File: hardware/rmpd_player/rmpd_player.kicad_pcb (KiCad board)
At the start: 2 copper layers, 59 parts, among them J1 POWER, J2 PROG, J3 LINE_OUT_INT, J4 LINE_OUT, J5 MICRO_SD, Q1 BC848, Q2 BC848, Q3 BC858, Q4 BC858, U1 DS3231M, U2 VS1011E, U3 LM1117-3.3, U4 ESP32-WROOM, Y1 12.288MHz

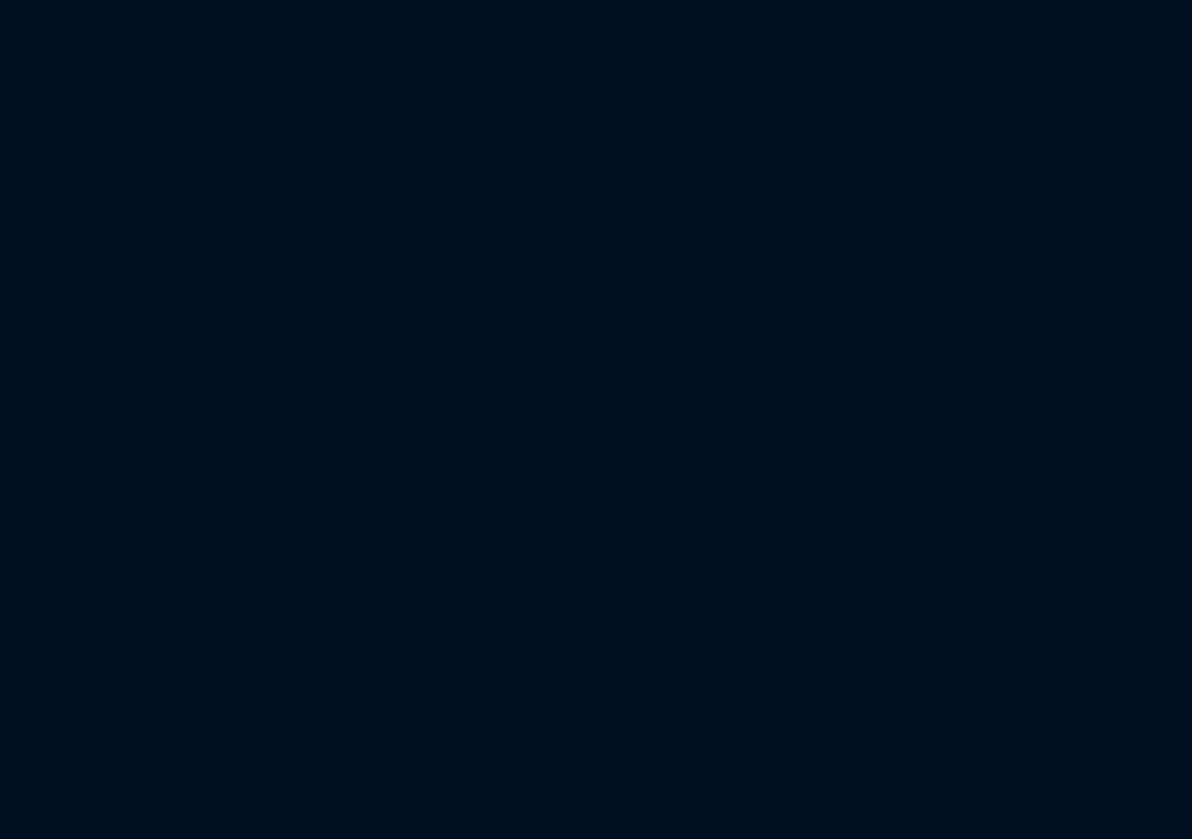
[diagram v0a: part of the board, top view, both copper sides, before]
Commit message: schematic op amp buffer; bom list
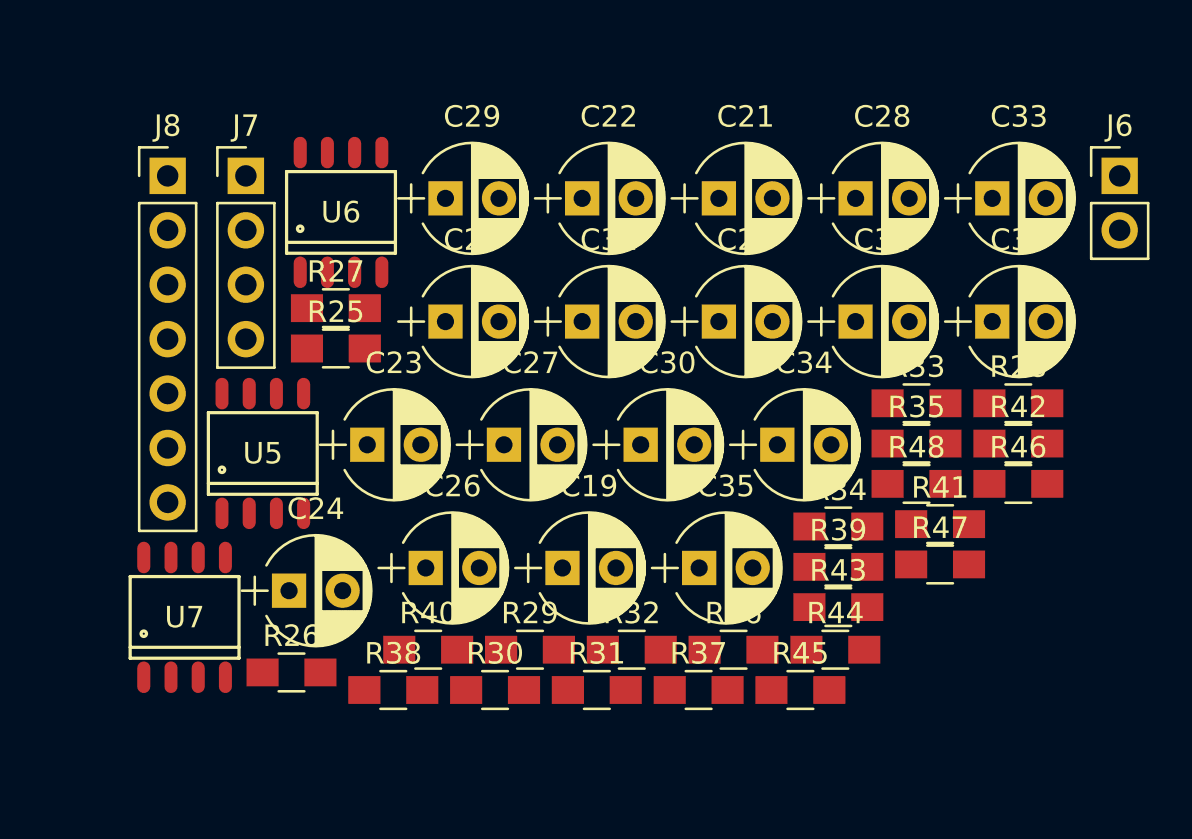
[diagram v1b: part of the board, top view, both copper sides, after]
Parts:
- added C19: 10.0, Capacitors_THT:CP_Radial_D5.0mm_P2.50mm, F.Cu at (195.5, 108.4)
- added C20: 10.0, Capacitors_THT:CP_Radial_D5.0mm_P2.50mm, F.Cu at (190.1, 96.9)
- added C21: 10.0, Capacitors_THT:CP_Radial_D5.0mm_P2.50mm, F.Cu at (202.8, 91.1)
- added C22: 10.0, Capacitors_THT:CP_Radial_D5.0mm_P2.50mm, F.Cu at (196.4, 91.1)
- added C23: 10.0, Capacitors_THT:CP_Radial_D5.0mm_P2.50mm, F.Cu at (186.4, 102.6)
- added C24: 10.0, Capacitors_THT:CP_Radial_D5.0mm_P2.50mm, F.Cu at (182.8, 109.5)
- added C25: 10.0, Capacitors_THT:CP_Radial_D5.0mm_P2.50mm, F.Cu at (202.8, 96.9)
- added C26: 10.0, Capacitors_THT:CP_Radial_D5.0mm_P2.50mm, F.Cu at (189.1, 108.4)
- added C27: 10.0, Capacitors_THT:CP_Radial_D5.0mm_P2.50mm, F.Cu at (192.8, 102.6)
- added C28: 10.0, Capacitors_THT:CP_Radial_D5.0mm_P2.50mm, F.Cu at (209.2, 91.1)
- added C29: 10.0, Capacitors_THT:CP_Radial_D5.0mm_P2.50mm, F.Cu at (190.1, 91.1)
- added C30: 10.0, Capacitors_THT:CP_Radial_D5.0mm_P2.50mm, F.Cu at (199.2, 102.6)
- added C31: 10.0, Capacitors_THT:CP_Radial_D5.0mm_P2.50mm, F.Cu at (196.4, 96.9)
- added C32: 10.0, Capacitors_THT:CP_Radial_D5.0mm_P2.50mm, F.Cu at (209.2, 96.9)
- added C33: 10.0, Capacitors_THT:CP_Radial_D5.0mm_P2.50mm, F.Cu at (215.6, 91.1)
- added C34: 10.0, Capacitors_THT:CP_Radial_D5.0mm_P2.50mm, F.Cu at (205.5, 102.6)
- added C35: 10.0, Capacitors_THT:CP_Radial_D5.0mm_P2.50mm, F.Cu at (201.9, 108.4)
- added C36: 10.0, Capacitors_THT:CP_Radial_D5.0mm_P2.50mm, F.Cu at (215.6, 96.9)
- added J6: POWER_INT, Pin_Headers:Pin_Header_Straight_1x02_Pitch2.54mm, F.Cu at (221.5, 90.1)
- added J7: LINE_OUT_INT_2, Pin_Headers:Pin_Header_Straight_1x04_Pitch2.54mm, F.Cu at (180.7, 90.1)
- added J8: RESERV, Pin_Headers:Pin_Header_Straight_1x07_Pitch2.54mm, F.Cu at (177.1, 90.1)
- added R25: 4k7, Resistors_SMD:R_0805_HandSoldering, F.Cu at (184.9, 98.1)
- added R26: 4k7, Resistors_SMD:R_0805_HandSoldering, F.Cu at (182.9, 113.3)
- added R27: 4k7, Resistors_SMD:R_0805_HandSoldering, F.Cu at (184.9, 96.3)
- added R28: 4k7, Resistors_SMD:R_0805_HandSoldering, F.Cu at (216.8, 100.7)
- added R29: 4k7, Resistors_SMD:R_0805_HandSoldering, F.Cu at (194.0, 112.2)
- added R30: 4k7, Resistors_SMD:R_0805_HandSoldering, F.Cu at (192.4, 114.1)
- added R31: 4k7, Resistors_SMD:R_0805_HandSoldering, F.Cu at (197.1, 114.1)
- added R32: 4k7, Resistors_SMD:R_0805_HandSoldering, F.Cu at (198.7, 112.2)
- added R33: 4k7, Resistors_SMD:R_0805_HandSoldering, F.Cu at (212.0, 100.7)
- added R34: 4k7, Resistors_SMD:R_0805_HandSoldering, F.Cu at (208.4, 106.5)
- added R35: 4k7, Resistors_SMD:R_0805_HandSoldering, F.Cu at (212.0, 102.6)
- added R36: 4k7, Resistors_SMD:R_0805_HandSoldering, F.Cu at (203.5, 112.2)
- added R37: 10k, Resistors_SMD:R_0805_HandSoldering, F.Cu at (201.9, 114.1)
- added R38: 10k, Resistors_SMD:R_0805_HandSoldering, F.Cu at (187.6, 114.1)
- added R39: 10k, Resistors_SMD:R_0805_HandSoldering, F.Cu at (208.4, 108.3)
- added R40: 10k, Resistors_SMD:R_0805_HandSoldering, F.Cu at (189.2, 112.2)
- added R41: 10k, Resistors_SMD:R_0805_HandSoldering, F.Cu at (213.1, 106.3)
- added R42: 10k, Resistors_SMD:R_0805_HandSoldering, F.Cu at (216.8, 102.6)
- added R43: 100k, Resistors_SMD:R_0805_HandSoldering, F.Cu at (208.4, 110.2)
- added R44: 100k, Resistors_SMD:R_0805_HandSoldering, F.Cu at (208.2, 112.2)
- added R45: 100k, Resistors_SMD:R_0805_HandSoldering, F.Cu at (206.6, 114.1)
- added R46: 100k, Resistors_SMD:R_0805_HandSoldering, F.Cu at (216.8, 104.5)
- added R47: 100k, Resistors_SMD:R_0805_HandSoldering, F.Cu at (213.1, 108.2)
- added R48: 100k, Resistors_SMD:R_0805_HandSoldering, F.Cu at (212.0, 104.5)
- added U5: RC4558, Power_Integrations:SO-8, F.Cu at (181.5, 103.0)
- added U6: RC4558, Power_Integrations:SO-8, F.Cu at (185.2, 91.8)
- added U7: RC4558, Power_Integrations:SO-8, F.Cu at (177.9, 110.7)
- J3: value LINE_OUT_INT -> LINE_OUT_INT_1
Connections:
- net Net-(C12-Pad1) renamed 5V
- C17 pad 2: Net-(C17-Pad2) -> OUT_R
- C18 pad 2: Net-(C18-Pad2) -> OUT_L
- J3 pad 1: Net-(C18-Pad2) -> Net-(C33-Pad2)
- J3 pad 4: Net-(C17-Pad2) -> Net-(C34-Pad2)
- J4 pad 1: Net-(C17-Pad2) -> Net-(C35-Pad2)
- J4 pad 2: Net-(C18-Pad2) -> Net-(C36-Pad2)
- Q1 pad 3: Net-(C17-Pad2) -> OUT_R
- Q2 pad 3: Net-(C18-Pad2) -> OUT_L
- R13 pad 1: Net-(C18-Pad2) -> OUT_L
- R14 pad 1: Net-(C17-Pad2) -> OUT_R
- R23 pad 1: TRANSIENT_MUTE -> Net-(Q4-Pad1)
- R23 pad 2: Net-(Q4-Pad1) -> TRANSIENT_MUTE
- R24 pad 1: TRANSIENT_MUTE -> VDD
- R24 pad 2: VDD -> TRANSIENT_MUTE

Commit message: op amps caps
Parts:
- added C37: 100n, Capacitors_SMD:C_0805_HandSoldering, F.Cu at (182.1, 78.4)
- added C38: 100n, Capacitors_SMD:C_0805_HandSoldering, F.Cu at (182.1, 80.2)
- added C39: 100n, Capacitors_SMD:C_0805_HandSoldering, F.Cu at (186.7, 78.4)
- D1: footprint Diodes_SMD:D_0805 -> Diodes_THT:D_A-405_P7.62mm_Horizontal
- moved D1 12.7 mm to (161.9, 86.2)
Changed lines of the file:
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@@
     (tracks 0)
     (zones 0)
-    (modules 107)
+    (modules 110)
     (nets 89)
   )
@@
     )
   )
-  (module Diodes_SMD:D_0805 (layer F.Cu)
-    (at 157.108001 97.937001)
-    (descr "Diode SMD in 0805 package http://datasheets.avx.com/schottky.pdf")
-    (tags "smd diode")
-    (attr smd)
-    (fp_text reference D1 (at 0 -1.6) (layer F.SilkS)
-      (effects (font (size 1 1) (thickness 0.15)))
-    )
-    (fp_text value 5.1V (at 0 1.7) (layer F.Fab)
-      (effects (font (size 1 1) (thickness 0.15)))
-    )
-    (fp_text user %R (at 0 -1.6) (layer F.Fab)
-      (effects (font (size 1 1) (thickness 0.15)))
-    )
-    (fp_line (start -1.6 -0.8) (end -1.6 0.8) (layer F.SilkS) (width 0.12))
-    (fp_line (start -1.7 0.88) (end -1.7 -0.88) (layer F.CrtYd) (width 0.05))
-    (fp_line (start 1.7 0.88) (end -1.7 0.88) (layer F.CrtYd) (width 0.05))
-    (fp_line (start 1.7 -0.88) (end 1.7 0.88) (layer F.CrtYd) (width 0.05))
-    (fp_line (start -1.7 -0.88) (end 1.7 -0.88) (layer F.CrtYd) (width 0.05))
-    (fp_line (start 0.2 0) (end 0.4 0) (layer F.Fab) (width 0.1))
-    (fp_line (start -0.1 0) (end -0.3 0) (layer F.Fab) (width 0.1))
-    (fp_line (start -0.1 -0.2) (end -0.1 0.2) (layer F.Fab) (width 0.1))
-    (fp_line (start 0.2 0.2) (end 0.2 -0.2) (layer F.Fab) (width 0.1))
-    (fp_line (start -0.1 0) (end 0.2 0.2) (layer F.Fab) (width 0.1))
-    (fp_line (start 0.2 -0.2) (end -0.1 0) (layer F.Fab) (width 0.1))
-    (fp_line (start -1 0.65) (end -1 -0.65) (layer F.Fab) (width 0.1))
-    (fp_line (start 1 0.65) (end -1 0.65) (layer F.Fab) (width 0.1))
-    (fp_line (start 1 -0.65) (end 1 0.65) (layer F.Fab) (width 0.1))
-    (fp_line (start -1 -0.65) (end 1 -0.65) (layer F.Fab) (width 0.1))
-    (fp_line (start -1.6 0.8) (end 1 0.8) (layer F.SilkS) (width 0.12))
-    (fp_line (start -1.6 -0.8) (end 1 -0.8) (layer F.SilkS) (width 0.12))
-    (pad 1 smd rect (at -1.05 0) (size 0.8 0.9) (layers F.Cu F.Paste F.Mask)
-      (net 55 5V))
-    (pad 2 smd rect (at 1.05 0) (size 0.8 0.9) (layers F.Cu F.Paste F.Mask)
-      (net 2 GND))
-    (model ${KISYS3DMOD}/Diodes_SMD.3dshapes/D_0805.wrl
-      (at (xyz 0 0 0))
-      (scale (xyz 1 1 1))
-      (rotate (xyz 0 0 0))
-    )
-  )
   (module Fuse_Holders_and_Fuses:Fuse_SMD1206_HandSoldering (layer F.Cu)
     (at 100.288 130.627001)
@@
       (net 78 "Net-(C35-Pad1)"))
   )
+  (module Capacitors_SMD:C_0805_HandSoldering (layer F.Cu)
+    (at 182.107001 78.380001)
+    (descr "Capacitor SMD 0805, hand soldering")
+    (tags "capacitor 0805")
+    (attr smd)
+    (fp_text reference C37 (at 0 -1.75) (layer F.SilkS)
+      (effects (font (size 1 1) (thickness 0.15)))
+    )
+    (fp_text value 100n (at 0 1.75) (layer F.Fab)
+      (effects (font (size 1 1) (thickness 0.15)))
+    )
+    (fp_line (start 2.25 0.87) (end -2.25 0.87) (layer F.CrtYd) (width 0.05))
+    (fp_line (start 2.25 0.87) (end 2.25 -0.88) (layer F.CrtYd) (width 0.05))
+    (fp_line (start -2.25 -0.88) (end -2.25 0.87) (layer F.CrtYd) (width 0.05))
+    (fp_line (start -2.25 -0.88) (end 2.25 -0.88) (layer F.CrtYd) (width 0.05))
+    (fp_line (start -0.5 0.85) (end 0.5 0.85) (layer F.SilkS) (width 0.12))
+    (fp_line (start 0.5 -0.85) (end -0.5 -0.85) (layer F.SilkS) (width 0.12))
+    (fp_line (start -1 -0.62) (end 1 -0.62) (layer F.Fab) (width 0.1))
+    (fp_line (start 1 -0.62) (end 1 0.62) (layer F.Fab) (width 0.1))
+    (fp_line (start 1 0.62) (end -1 0.62) (layer F.Fab) (width 0.1))
+    (fp_line (start -1 0.62) (end -1 -0.62) (layer F.Fab) (width 0.1))
+    (fp_text user %R (at 0 -1.75) (layer F.Fab)
+      (effects (font (size 1 1) (thickness 0.15)))
+    )
+    (pad 2 smd rect (at 1.25 0) (size 1.5 1.25) (layers F.Cu F.Paste F.Mask)
+      (net 2 GND))
+    (pad 1 smd rect (at -1.25 0) (size 1.5 1.25) (layers F.Cu F.Paste F.Mask)
+      (net 55 5V))
+    (model Capacitors_SMD.3dshapes/C_0805.wrl
+      (at (xyz 0 0 0))
+      (scale (xyz 1 1 1))
+      (rotate (xyz 0 0 0))
+    )
+  )
+  (module Capacitors_SMD:C_0805_HandSoldering (layer F.Cu)
+    (at 182.107001 80.200001)
+    (descr "Capacitor SMD 0805, hand soldering")
+    (tags "capacitor 0805")
+    (attr smd)
+    (fp_text reference C38 (at 0 -1.75) (layer F.SilkS)
+      (effects (font (size 1 1) (thickness 0.15)))
+    )
+    (fp_text value 100n (at 0 1.75) (layer F.Fab)
+      (effects (font (size 1 1) (thickness 0.15)))
+    )
+    (fp_text user %R (at 0 -1.75) (layer F.Fab)
+      (effects (font (size 1 1) (thickness 0.15)))
+    )
+    (fp_line (start -1 0.62) (end -1 -0.62) (layer F.Fab) (width 0.1))
+    (fp_line (start 1 0.62) (end -1 0.62) (layer F.Fab) (width 0.1))
+    (fp_line (start 1 -0.62) (end 1 0.62) (layer F.Fab) (width 0.1))
+    (fp_line (start -1 -0.62) (end 1 -0.62) (layer F.Fab) (width 0.1))
+    (fp_line (start 0.5 -0.85) (end -0.5 -0.85) (layer F.SilkS) (width 0.12))
+    (fp_line (start -0.5 0.85) (end 0.5 0.85) (layer F.SilkS) (width 0.12))
+    (fp_line (start -2.25 -0.88) (end 2.25 -0.88) (layer F.CrtYd) (width 0.05))
+    (fp_line (start -2.25 -0.88) (end -2.25 0.87) (layer F.CrtYd) (width 0.05))
+    (fp_line (start 2.25 0.87) (end 2.25 -0.88) (layer F.CrtYd) (width 0.05))
+    (fp_line (start 2.25 0.87) (end -2.25 0.87) (layer F.CrtYd) (width 0.05))
+    (pad 1 smd rect (at -1.25 0) (size 1.5 1.25) (layers F.Cu F.Paste F.Mask)
+      (net 55 5V))
+    (pad 2 smd rect (at 1.25 0) (size 1.5 1.25) (layers F.Cu F.Paste F.Mask)
+      (net 2 GND))
+    (model Capacitors_SMD.3dshapes/C_0805.wrl
+      (at (xyz 0 0 0))
+      (scale (xyz 1 1 1))
+      (rotate (xyz 0 0 0))
+    )
+  )
+  (module Capacitors_SMD:C_0805_HandSoldering (layer F.Cu)
+    (at 186.657001 78.380001)
+    (descr "Capacitor SMD 0805, hand soldering")
+    (tags "capacitor 0805")
+    (attr smd)
+    (fp_text reference C39 (at 0 -1.75) (layer F.SilkS)
+      (effects (font (size 1 1) (thickness 0.15)))
+    )
+    (fp_text value 100n (at 0 1.75) (layer F.Fab)
+      (effects (font (size 1 1) (thickness 0.15)))
+    )
+    (fp_line (start 2.25 0.87) (end -2.25 0.87) (layer F.CrtYd) (width 0.05))
+    (fp_line (start 2.25 0.87) (end 2.25 -0.88) (layer F.CrtYd) (width 0.05))
+    (fp_line (start -2.25 -0.88) (end -2.25 0.87) (layer F.CrtYd) (width 0.05))
+    (fp_line (start -2.25 -0.88) (end 2.25 -0.88) (layer F.CrtYd) (width 0.05))
+    (fp_line (start -0.5 0.85) (end 0.5 0.85) (layer F.SilkS) (width 0.12))
+    (fp_line (start 0.5 -0.85) (end -0.5 -0.85) (layer F.SilkS) (width 0.12))
+    (fp_line (start -1 -0.62) (end 1 -0.62) (layer F.Fab) (width 0.1))
+    (fp_line (start 1 -0.62) (end 1 0.62) (layer F.Fab) (width 0.1))
+    (fp_line (start 1 0.62) (end -1 0.62) (layer F.Fab) (width 0.1))
+    (fp_line (start -1 0.62) (end -1 -0.62) (layer F.Fab) (width 0.1))
+    (fp_text user %R (at 0 -1.75) (layer F.Fab)
+      (effects (font (size 1 1) (thickness 0.15)))
+    )
+    (pad 2 smd rect (at 1.25 0) (size 1.5 1.25) (layers F.Cu F.Paste F.Mask)
+      (net 2 GND))
+    (pad 1 smd rect (at -1.25 0) (size 1.5 1.25) (layers F.Cu F.Paste F.Mask)
+      (net 55 5V))
+    (model Capacitors_SMD.3dshapes/C_0805.wrl
+      (at (xyz 0 0 0))
+      (scale (xyz 1 1 1))
+      (rotate (xyz 0 0 0))
+    )
+  )
+  (module Diodes_THT:D_A-405_P7.62mm_Horizontal (layer F.Cu)
+    (at 161.925 86.233)
+    (descr "D, A-405 series, Axial, Horizontal, pin pitch=7.62mm, , length*diameter=5.2*2.7mm^2, , http://www.diodes.com/_files/packages/A-405.pdf")
+    (tags "D A-405 series Axial Horizontal pin pitch 7.62mm  length 5.2mm diameter 2.7mm")
+    (fp_text reference D1 (at 3.81 -2.41) (layer F.SilkS)
+      (effects (font (size 1 1) (thickness 0.15)))
+    )
+    (fp_text value 5.1V (at 3.81 2.41) (layer F.Fab)
+      (effects (font (size 1 1) (thickness 0.15)))
+    )
+    (fp_line (start 8.8 -1.7) (end -1.15 -1.7) (layer F.CrtYd) (width 0.05))
+    (fp_line (start 8.8 1.7) (end 8.8 -1.7) (layer F.CrtYd) (width 0.05))
+    (fp_line (start -1.15 1.7) (end 8.8 1.7) (layer F.CrtYd) (width 0.05))
+    (fp_line (start -1.15 -1.7) (end -1.15 1.7) (layer F.CrtYd) (width 0.05))
+    (fp_line (start 1.99 -1.41) (end 1.99 1.41) (layer F.SilkS) (width 0.12))
+    (fp_line (start 6.54 0) (end 6.47 0) (layer F.SilkS) (width 0.12))
+    (fp_line (start 1.08 0) (end 1.15 0) (layer F.SilkS) (width 0.12))
+    (fp_line (start 6.47 -1.41) (end 1.15 -1.41) (layer F.SilkS) (width 0.12))
+    (fp_line (start 6.47 1.41) (end 6.47 -1.41) (layer F.SilkS) (width 0.12))
+    (fp_line (start 1.15 1.41) (end 6.47 1.41) (layer F.SilkS) (width 0.12))
+    (fp_line (start 1.15 -1.41) (end 1.15 1.41) (layer F.SilkS) (width 0.12))
+    (fp_line (start 1.99 -1.35) (end 1.99 1.35) (layer F.Fab) (width 0.1))
+    (fp_line (start 7.62 0) (end 6.41 0) (layer F.Fab) (width 0.1))
+    (fp_line (start 0 0) (end 1.21 0) (layer F.Fab) (width 0.1))
+    (fp_line (start 6.41 -1.35) (end 1.21 -1.35) (layer F.Fab) (width 0.1))
+    (fp_line (start 6.41 1.35) (end 6.41 -1.35) (layer F.Fab) (width 0.1))
+    (fp_line (start 1.21 1.35) (end 6.41 1.35) (layer F.Fab) (width 0.1))
+    (fp_line (start 1.21 -1.35) (end 1.21 1.35) (layer F.Fab) (width 0.1))
+    (fp_text user %R (at 3.81 0) (layer F.Fab)
+      (effects (font (size 1 1) (thickness 0.15)))
+    )
+    (pad 2 thru_hole oval (at 7.62 0) (size 1.8 1.8) (drill 0.9) (layers *.Cu *.Mask)
+      (net 2 GND))
+    (pad 1 thru_hole rect (at 0 0) (size 1.8 1.8) (drill 0.9) (layers *.Cu *.Mask)
+      (net 55 5V))
+    (model ${KISYS3DMOD}/Diodes_THT.3dshapes/D_A-405_P7.62mm_Horizontal.wrl
+      (at (xyz 0 0 0))
+      (scale (xyz 0.393701 0.393701 0.393701))
+      (rotate (xyz 0 0 0))
+    )
+  )
 )

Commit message: pcb
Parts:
- R25, R26, R28, R30, R32, R34, R36, R37, R38, R39, R40, R41, R42, R43, R44, R45, R46, R47, R48, U5, U6, U7: moved to B.Cu
- moved R42 176.9 mm to (40.6, 118.8), turned to 270 degrees
- moved C36 171.8 mm to (45.8, 123.2)
- moved R48 165.6 mm to (48.3, 128.9), turned to 90 degrees
- moved R35 165.5 mm to (47.0, 114.3)
- moved R47 162.4 mm to (52.1, 128.9), turned to 90 degrees
- moved R28 160.3 mm to (56.5, 103.5), turned to 270 degrees
- moved R33 158.6 mm to (54.0, 114.3), turned to 180 degrees
- moved C30 156.7 mm to (43.2, 117.5), turned to 270 degrees
- moved R36 156.5 mm to (47.0, 114.3), turned to 180 degrees
- moved R34 154.6 mm to (54.0, 114.3)
- moved R41 153.3 mm to (60.3, 118.7), turned to 270 degrees
- moved C35 148.0 mm to (54.6, 123.2), turned to 180 degrees
- moved R46 147.4 mm to (72.4, 134.0), turned to 180 degrees
- moved C28 145.2 mm to (67.3, 121.9), turned to 270 degrees
- moved C19 143.7 mm to (52.7, 92.8), turned to 270 degrees
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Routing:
- net GND: track 0.00 -> 123.7 mm, vias 0 -> 2
- net OUT_R: track 0.00 -> 40.9 mm
- net OUT_L: track 0.00 -> 37.5 mm
- net 5V: track 0.00 -> 21.3 mm, vias 0 -> 2
- net Net-(C24-Pad1): track 0.00 -> 15.2 mm
- net Net-(C23-Pad1): track 0.00 -> 15.0 mm
- net Net-(C22-Pad1): track 0.00 -> 14.6 mm
- net Net-(C21-Pad1): track 0.00 -> 14.6 mm
- net Net-(C33-Pad1): track 0.00 -> 11.0 mm, vias 0 -> 1
- net Net-(C35-Pad2): track 0.00 -> 9.94 mm
- net Net-(C36-Pad2): track 0.00 -> 9.92 mm
- net Net-(C34-Pad1): track 0.00 -> 8.79 mm, vias 0 -> 1
- net Net-(C35-Pad1): track 0.00 -> 8.52 mm, vias 0 -> 1
- net Net-(C28-Pad2): track 0.00 -> 7.96 mm
- net Net-(C30-Pad2): track 0.00 -> 7.47 mm
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
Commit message: moar pcb
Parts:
- added REF**: 1pin, Connectors:1pin, F.Cu at (34.9, 93.3)
- added REF**: 1pin, Connectors:1pin, F.Cu at (34.9, 137.8)
- C1, C2, C4, C5, C6, C7, C9, R1, U2: moved to B.Cu
- R25: moved to F.Cu
- moved C1 119.0 mm to (89.6, 92.1), turned to 180 degrees
- moved C7 114.8 mm to (88.9, 104.1), turned to 270 degrees
- moved D1 113.3 mm to (114.9, 123.2), turned to 270 degrees
- moved C5 112.5 mm to (91.4, 110.5), turned to 270 degrees
- moved C4 105.0 mm to (99.7, 110.5)
- moved C6 94.3 mm to (104.8, 104.8), turned to 270 degrees
- moved J1 92.1 mm to (106.0, 127.0), turned to 90 degrees
- moved C9 87.3 mm to (95.9, 112.4), turned to 270 degrees
- moved C2 85.0 mm to (102.3, 92.1)
- moved U2 78.3 mm to (96.5, 102.9)
- moved J5 77.7 mm to (137.2, 137.2)
- moved F1 44.8 mm to (108.0, 123.2)
- moved Y1 39.2 mm to (93.5, 92.1)
- moved R1 36.5 mm to (95.9, 94.6)
- moved BT1 35.2 mm to (116.2, 43.8)
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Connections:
- C4 pad 1: VDD -> VDDA
- C5 pad 1: VDD -> VDDA
- U2 pad 38: VDD -> VDDA
- U2 pad 43: VDD -> VDDA
- U2 pad 45: VDD -> VDDA
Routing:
- net GND: track 123.7 -> 216.8 mm, vias 2 -> 3
- net 5V: track 21.3 -> 78.3 mm, vias 2 -> 5
- net VDD: track 0.00 -> 37.4 mm, vias 0 -> 4
- net OUT_R: track 40.9 -> 68.9 mm
- net Net-(C31-Pad1): track 0.00 -> 22.3 mm, vias 0 -> 1
- net Net-(C19-Pad1): track 0.00 -> 17.1 mm
- net Net-(C25-Pad2): track 0.00 -> 13.0 mm
- net Net-(C20-Pad1): track 0.00 -> 12.8 mm
- net Net-(C32-Pad1): track 0.00 -> 12.4 mm
- net Net-(C1-Pad1): track 0.00 -> 10.1 mm
- net Net-(C2-Pad1): track 0.00 -> 9.92 mm
- net Net-(C26-Pad2): track 0.00 -> 7.70 mm
- net Net-(C32-Pad2): track 0.00 -> 6.92 mm
- net Net-(C31-Pad2): track 0.00 -> 6.86 mm
- net OUT_L: track 37.5 -> 43.4 mm
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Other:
- board outline added: 119.4 x 52.1 mm
- net class power added: clearance 0.2, trace_width 0.4, via_dia 0.8, via_drill 0.4
- board text added: "BOTTOM"
- board text added: "TOP"
